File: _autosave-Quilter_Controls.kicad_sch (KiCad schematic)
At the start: 16 parts, among them J1 Conn_01x10_Male, J10 Conn_01x04_Male, J2 Conn_01x10_Male, J3 Conn_01x10_Male, J4 Audio_In, J5 Audio_Out, J6 Audio_Mix, J7 Freq_V_Oct, J8 Freq_CV, J9 Conn_02x04_Top_Bottom

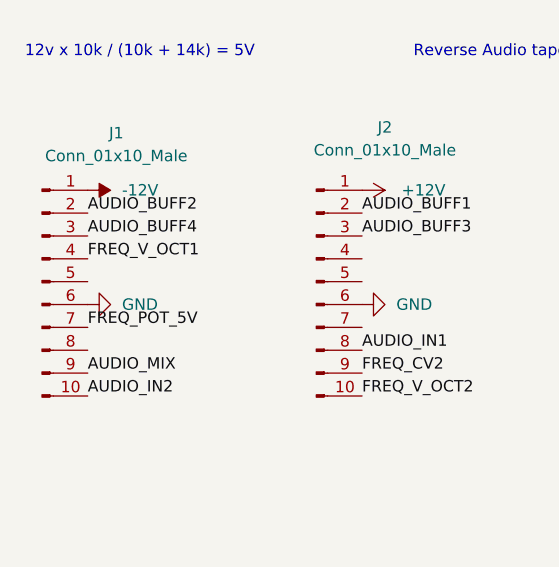
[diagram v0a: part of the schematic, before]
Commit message: Re-routed Controls board
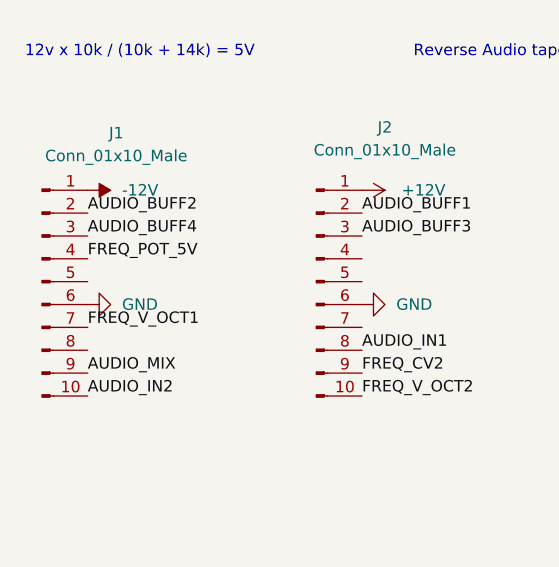
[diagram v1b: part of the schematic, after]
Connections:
- net FREQ_POT_5V: now also J1.4 (Pin_4); no longer J1.7 (Pin_7)
- net FREQ_V_OCT1: now also J1.7 (Pin_7); no longer J1.4 (Pin_4)
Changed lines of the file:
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@@
     (effects (font (size 1.27 1.27)) (justify left bottom))
   )
-  (label "FREQ_V_OCT1" (at 32.385 74.295 0)
+  (label "FREQ_V_OCT1" (at 32.385 81.915 0)
     (effects (font (size 1.27 1.27)) (justify left bottom))
   )
@@
     (effects (font (size 1.27 1.27)) (justify left bottom))
   )
-  (label "FREQ_POT_5V" (at 32.385 81.915 0)
+  (label "FREQ_POT_5V" (at 32.385 74.295 0)
     (effects (font (size 1.27 1.27)) (justify left bottom))
   )
